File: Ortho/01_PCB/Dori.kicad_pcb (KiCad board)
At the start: 2 copper layers, 306.4 x 111.1 mm, 206 parts, among them J1 TYPE-C-31-M12_13, J2 AVR-ISP-6_mod, J3 4PIN, J4 4PIN, J5 TYPE-C-31-M12_13, J6 AVR-ISP-6_mod, K1 KEYSW, K10 KEYSW, K11 KEYSW, K12 KEYSW, K13 KEYSW, K14 KEYSW, K15 KEYSW, K16 KEYSW, K17 KEYSW, K18 KEYSW, K19 KEYSW, K2 KEYSW, K20 KEYSW, K21 KEYSW, K22 KEYSW, K23 KEYSW, K24 KEYSW, K25 KEYSW, K26 KEYSW, K27 KEYSW, K28 KEYSW, K29 KEYSW, K3 KEYSW, K30 KEYSW, K31 KEYSW, K32 KEYSW, K33 KEYSW, K34 KEYSW, K35 KEYSW, K36 KEYSW, K37 KEYSW, K38 KEYSW, K39 KEYSW, K4 KEYSW, K40 KEYSW, K41 KEYSW, K42 KEYSW, K43 KEYSW, K44 KEYSW, K45 KEYSW, K46 KEYSW, K47 KEYSW, K48 KEYSW, K49 KEYSW, K5 KEYSW, K50 KEYSW, K51 KEYSW, K52 KEYSW, K53 KEYSW, K54 KEYSW, K55 KEYSW, K56 KEYSW, K6 KEYSW, K7 KEYSW, K8 KEYSW, K9 KEYSW, SW1 SW_PUSH, SW10 Rotary_Encoder_Switch, SW2 SW_PUSH, SW3 Rotary_Encoder_Switch, SW4 Rotary_Encoder_Switch, SW5 Rotary_Encoder_Switch, SW6 Rotary_Encoder_Switch, SW7 Rotary_Encoder_Switch, SW8 Rotary_Encoder_Switch, SW9 Rotary_Encoder_Switch, U1 ATMEGA32U4, U10 HOLE, U11 HOLE, U12 ATMEGA32U4, U13 HOLE, U14 HOLE, U15 HOLE, U16 HOLE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

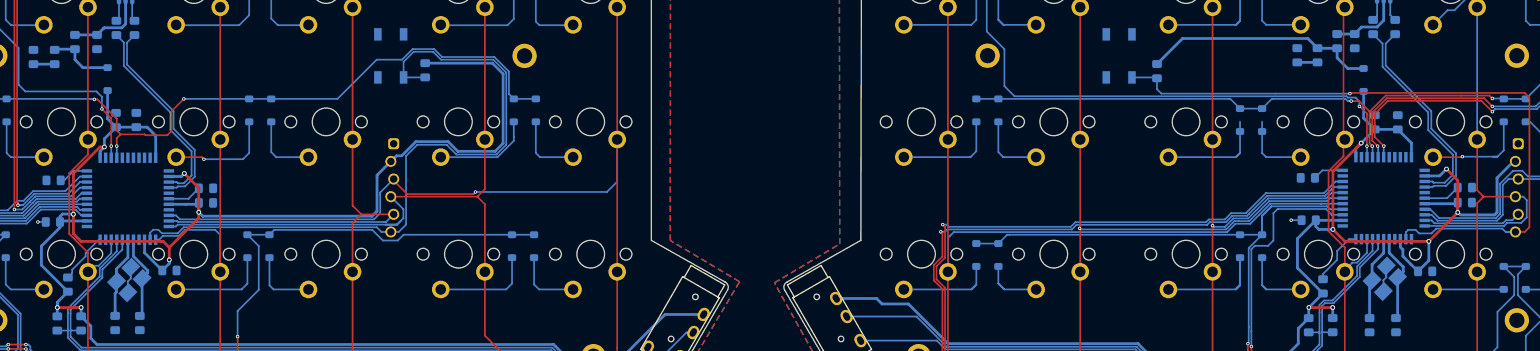
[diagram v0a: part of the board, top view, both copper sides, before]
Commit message: Rerouted power lines
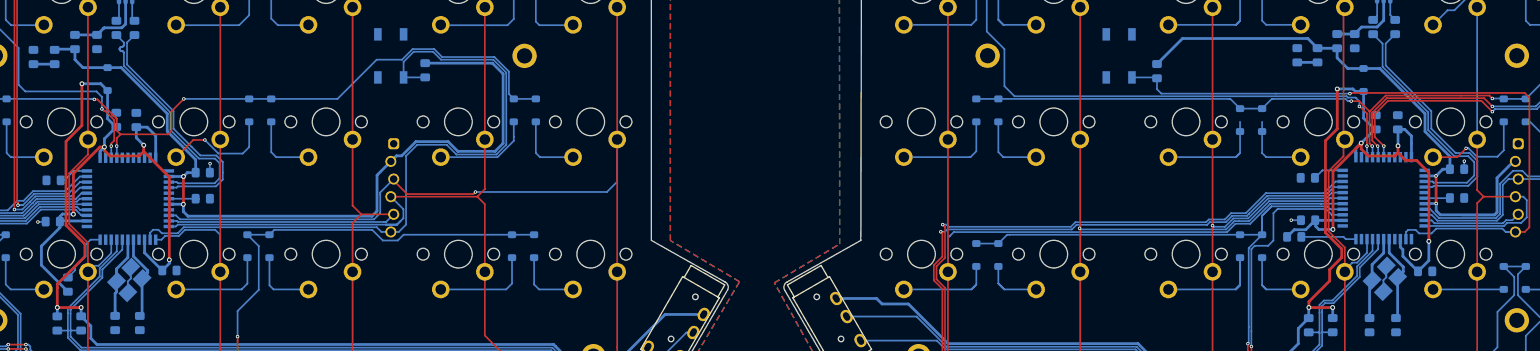
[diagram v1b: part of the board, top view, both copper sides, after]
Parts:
- C1, C10, C2, C3, C4, C7, C8, C9, CESD1, CESD2: value 100nF -> .1uF
- R13, R14: value 10K -> 10k
- R4, R9: value 1K -> 1k
- R5, R6, R7, R8: value 4.7K -> 4.7k
- RCC1, RCC2, RCC3, RCC4: value 5.1K -> 5.1k
- moved C5 22.7 mm to (165.6, 78.8), turned to 0 degrees
- moved C11 22.6 mm to (346.2, 78.2), turned to 0 degrees
- moved C4 17.6 mm to (153.2, 71.2), turned to 90 degrees
- moved C10 17.3 mm to (334.5, 71.5), turned to 90 degrees
- moved C2 17.2 mm to (144.0, 85.8), turned to 180 degrees
- moved C9 17.1 mm to (324.8, 85.6), turned to 180 degrees
- moved R14 8.24 mm to (322.8, 88.0), turned to 0 degrees
- moved C12 1.87 mm to (346.2, 82.4)
- moved C6 1.56 mm to (165.6, 82.5)
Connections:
- C11 pad 1: VDD -> +5VA
- C5 pad 1: VCC -> +5V
- J2 pad 2: VCC -> +5V
- J6 pad 2: VDD -> +5VA
- RSW1 pad 2: VCC -> +5V
- U1 pad 2: VCC -> +5V
- U1 pad 7: VCC -> +5V
- U12 pad 2: VDD -> +5VA
- U12 pad 7: VDD -> +5VA
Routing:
- net +5V: track 9.65 -> 119.2 mm, vias 0 -> 2
- net +5VA: track 33.9 -> 96.7 mm, vias 0 -> 2
- net VCC: track 281.9 -> 228.0 mm
- net VDD: track 213.7 -> 199.7 mm
- net Da-: track 28.5 -> 36.6 mm
- net Da+: track 29.3 -> 36.6 mm
- net Db-: track 29.6 -> 35.2 mm
- net Db+: track 30.3 -> 35.9 mm
- net Net-(C12-Pad1): track 5.39 -> 3.65 mm
- net GND: track 19.8 -> 21.1 mm, vias 5 -> 6
- net GNDA: track 19.7 -> 20.9 mm, vias 3 -> 4
- net Net-(D15-Pad2): track 16.4 -> 17.1 mm
- net HDETECT: track 7.47 -> 8.17 mm
- net Net-(C6-Pad1): track 4.94 -> 4.38 mm
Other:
- board text added: "Encoder D"

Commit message: Moved USB port
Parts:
- moved RCC2 38.6 mm to (200.2, 47.1)
- moved R9 38.1 mm to (288.0, 61.9)
- moved LED1 38.1 mm to (179.3, 62.0)
- moved R4 38.1 mm to (182.4, 62.0)
- moved LED2 38.1 mm to (285.1, 61.9)
- moved C13 38.1 mm to (180.1, 47.1)
- moved CESD2 38.1 mm to (293.4, 59.8)
- moved F2 38.1 mm to (290.8, 59.8)
- moved J5 38.1 mm to (297.7, 49.2)
- moved R10 38.1 mm to (296.0, 57.8)
- moved R11 38.1 mm to (299.2, 57.8)
- moved R16 38.1 mm to (287.7, 47.0)
- moved RCC3 38.1 mm to (290.8, 47.0)
- moved RCC4 38.1 mm to (304.4, 47.0)
- moved U3 38.1 mm to (192.6, 52.9)
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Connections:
- RSW2 pad 2: +5VA -> VDD
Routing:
- net VDD: track 199.7 -> 259.2 mm, vias 7 -> 8
- net Db-: track 35.2 -> 80.9 mm
- net Db+: track 35.9 -> 80.9 mm
- net ISP_RSTb: track 99.4 -> 137.7 mm
- net ISP_RSTa: track 97.8 -> 60.6 mm
- net +5VA: track 96.7 -> 117.6 mm
- net +5V: track 119.2 -> 139.6 mm
- net Da-: track 36.6 -> 51.0 mm
- net Da+: track 36.6 -> 51.0 mm
- net GNDA: track 20.9 -> 31.8 mm, vias 4 -> 6
- net GND: track 21.1 -> 30.4 mm, vias 6 -> 5
- net row1a: track 135.9 -> 128.0 mm, vias 3 -> 5
- net SDAa: track 113.9 -> 119.8 mm
- net SCLb: track 89.2 -> 93.0 mm
- net XTAL1b: track 12.6 -> 9.61 mm
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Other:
- outline, holes or cut-outs redrawn
- net class Power added: clearance 0.13, trace_width 0.4, via_dia 0.7, via_drill 0.4
- net class Thick removed
- board text added: "github.com/dierickdie Dori Rev 1.1"
- board text removed: "Dori Rev 1.1"
- board text removed: "github.com/dierickdie"
